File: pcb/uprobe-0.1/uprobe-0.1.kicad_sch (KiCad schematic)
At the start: 99 parts, among them J1 uConsoleEXT, J2 Conn_02x05_Odd_Even, J3 Conn_02x05_Odd_Even, J4 JST_SH_BM03B-SRSS, J5 Conn_01x02, J7 Conn_01x04, Q1 BSS138, Q7 DMG1024UV, Q8 DMG1023UV, SW1 XUNPU TS-1088-AR02016, SW2 XUNPU TS-1088-AR02016, U1 ATmega8A-M, U10 74LVC2T45DC, U11 74LVC2T45DC, U12 74LVC2T45DC, U2 AMS1117-3.3, U3 AP22653, U4 AP22653, U5 STM32F103CBUx, U6 74LVC2T45DC, U7 74LVC2T45DC, U8 74LVC2T45DC, U9 74LVC2T45DC, Y1 ABM8-12.000MHZ-B2-T, Y2 ABM8-8.000MHZ-B2-T

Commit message: layout update
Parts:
- added JP2: SolderJumper_3_Bridged12, Jumper:SolderJumper-3_P2.0mm_Open_TrianglePad1.0x1.5mm, symbol Jumper:SolderJumper_3_Bridged12
- added JP3: SolderJumper_2_Open, Jumper:SolderJumper-2_P1.3mm_Open_TrianglePad1.0x1.5mm, symbol Jumper:SolderJumper_2_Open
- added LD3, LD4: XL-3210SURUGC, uprobe:XL-3210SURUGC, symbol Device:LED_Dual_AKAK
- added R43, R44, R45, R46: 270, Resistor_SMD:R_0603_1608Metric, symbol Device:R
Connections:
- net BM_LED0: now also R43.2
- net BM_LED1: now also R45.2, R46.2
- net BM_LED2: now also R44.2
- net GND: now also JP2.1 (A), LD3.2 (K1), LD3.4 (K2), LD4.2 (K1), LD4.4 (K2); no longer J3.9 (Pin_9)
- net RST: now also RN2.3 (R3.1); no longer RN2.5 (R4.2)
- net RXD: now also RN2.2 (R2.1), JP2.3 (B); no longer RN2.7 (R2.2)
- net TCK: now also RN1.3 (R3.1); no longer RN1.6 (R3.2)
- net TDI: now also RN1.1 (R1.1); no longer RN1.8 (R1.2)
- net TDO: now also RN1.2 (R2.1); no longer RN1.7 (R2.2)
- net TMS: now also RN1.4 (R4.1); no longer RN1.5 (R4.2)
- net TPWR: now also RN2.4 (R4.1); no longer RN2.6 (R3.2)
- net TXD: now also RN2.1 (R1.1), JP3.2 (B); no longer RN2.8 (R1.2)
- net xRST: now also RN2.6 (R3.2); no longer RN2.4 (R4.1)
- net xRXD: now also RN2.7 (R2.2); no longer RN2.2 (R2.1)
- net xTCK: now also RN1.6 (R3.2); no longer RN1.3 (R3.1)
- net xTDI: now also RN1.8 (R1.2); no longer RN1.1 (R1.1)
- net xTDO: now also RN1.7 (R2.2); no longer RN1.2 (R2.1)
- net xTMS: now also RN1.5 (R4.2); no longer RN1.4 (R4.1)
- net xTPWR: now also RN2.5 (R4.2); no longer RN2.3 (R3.1)
- net xTXD: now also RN2.8 (R1.2); no longer RN2.1 (R1.1)
- net at J3.7 (Pin_7): now also JP3.1 (A)
- net TPWR_DTCT: now reaches C18.1, R33.1, R34.2, U5.18 (PB0)
- net UASP_MISO renamed xUASP_MISO
- net UASP_MISO* renamed iUASP_MISO
- net UASP_MOSI renamed xUASP_MOSI
- net UASP_MOSI* renamed iUASP_MOSI
- net UASP_RST renamed xUASP_RST
- net UASP_RST* renamed iUASP_RST
- net UASP_RX renamed xUASP_RX
- net UASP_RX* renamed iUASP_RX
- net UASP_SCK renamed xUASP_SCK
- net UASP_SCK* renamed iUASP_SCK
- net UASP_TX renamed xUASP_TX
- net UASP_TX* renamed iUASP_TX
- new net: LD3.1 (A1), R43.1
- new net: LD3.3 (A2), R44.1
- new net: J3.9 (Pin_9), JP2.2 (C)
- new net: LD4.3 (A2), R46.1
- new net: LD4.1 (A1), R45.1
- no-connect marks 31 -> 30
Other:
- note removed: "TODO: LEDS!!!"
- moved on the sheet: J7, LD1, R30, R31, R5, R6, RN1, RN2

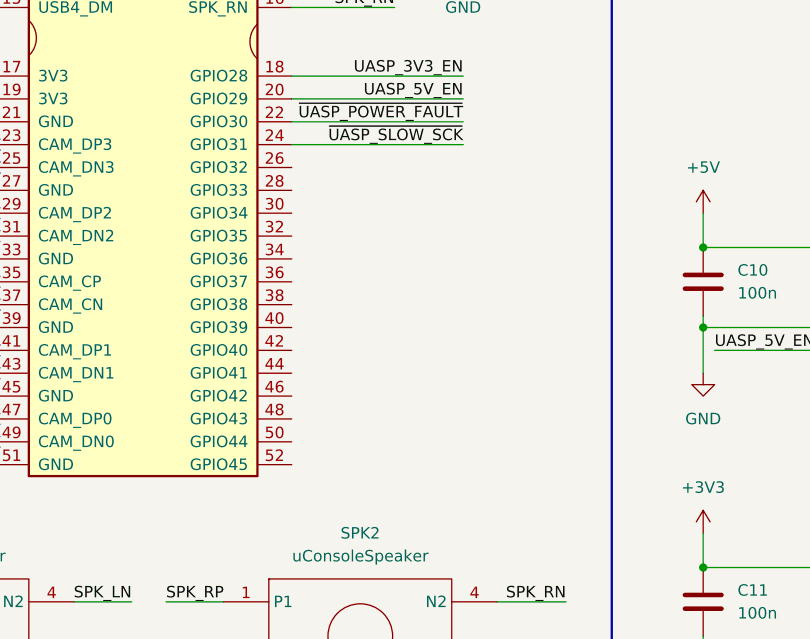
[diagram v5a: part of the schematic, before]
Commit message: additional gpio
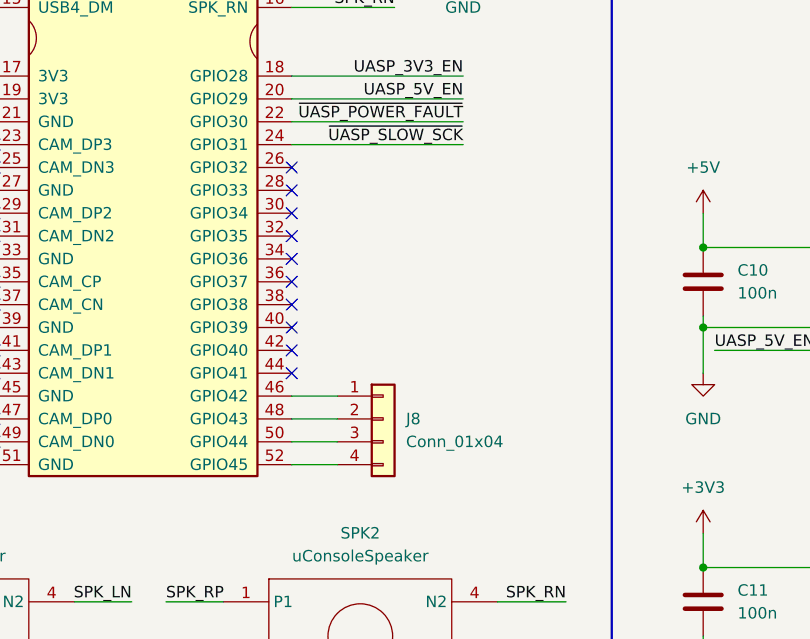
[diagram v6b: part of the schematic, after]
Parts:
- added J8: Conn_01x04, Connector_PinHeader_2.54mm:PinHeader_1x04_P2.54mm_Vertical, symbol Connector_Generic:Conn_01x04
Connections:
- net at J1.46 (GPIO42): now also J8.1 (Pin_1)
- net at J1.48 (GPIO43): now also J8.2 (Pin_2)
- net at J1.50 (GPIO44): now also J8.3 (Pin_3)
- net at J1.52 (GPIO45): now also J8.4 (Pin_4)
- no-connect marks 30 -> 40
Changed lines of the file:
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@@
 	)
 	(no_connect
+		(at 77.47 85.09)
+	)
+	(no_connect
 		(at 217.17 68.58)
 	)
@@
 	)
 	(no_connect
+		(at 77.47 74.93)
+	)
+	(no_connect
 		(at 44.45 64.77)
 	)
 	(no_connect
+		(at 77.47 69.85)
+	)
+	(no_connect
+		(at 77.47 87.63)
+	)
+	(no_connect
 		(at 247.65 78.74)
 	)
@@
 	)
 	(no_connect
+		(at 77.47 82.55)
+	)
+	(no_connect
 		(at 247.65 101.6)
 	)
@@
 	)
 	(no_connect
+		(at 77.47 90.17)
+	)
+	(no_connect
 		(at 247.65 81.28)
 	)
 	(no_connect
+		(at 77.47 67.31)
+	)
+	(no_connect
 		(at 151.13 229.87)
 	)
 	(no_connect
+		(at 77.47 80.01)
+	)
+	(no_connect
 		(at 151.13 196.85)
 	)
@@
 	)
 	(no_connect
+		(at 77.47 72.39)
+	)
+	(no_connect
 		(at 247.65 96.52)
 	)
@@
 	)
 	(no_connect
+		(at 77.47 77.47)
+	)
+	(no_connect
 		(at 186.69 217.17)
 	)
@@
 	(wire
 		(pts
+			(xy 77.47 95.25) (xy 82.55 95.25)
+		)
+		(stroke
+			(width 0)
+			(type default)
+		)
+	)
+	(wire
+		(pts
 			(xy 361.95 203.2) (xy 361.95 207.01)
 		)
@@
 	(wire
 		(pts
+			(xy 77.47 97.79) (xy 82.55 97.79)
+		)
+		(stroke
+			(width 0)
+			(type default)
+		)
+	)
+	(wire
+		(pts
 			(xy 30.48 85.09) (xy 30.48 92.71)
 		)
@@
 	(wire
 		(pts
+			(xy 77.47 92.71) (xy 82.55 92.71)
+		)
+		(stroke
+			(width 0)
+			(type default)
+		)
+	)
+	(wire
+		(pts
 			(xy 336.55 36.83) (xy 336.55 57.15)
 		)
@@
 	(wire
 		(pts
+			(xy 77.47 100.33) (xy 82.55 100.33)
+		)
+		(stroke
+			(width 0)
+			(type default)
+		)
+	)
+	(wire
+		(pts
 			(xy 321.31 31.75) (xy 321.31 29.21)
 		)
@@
 					(unit 1)
 				)
+			)
+		)
+	)
+	(symbol
+		(lib_id "Connector_Generic:Conn_01x04")
+		(at 87.63 95.25 0)
+		(unit 1)
+		(exclude_from_sim no)
+		(in_bom yes)
+		(on_board yes)
+		(dnp no)
+		(fields_autoplaced yes)
+		(property "Reference" "J8"
+			(at 90.17 95.2499 0)
+			(effects
+				(font
+					(size 1.27 1.27)
+				)
+				(justify left)
+			)
+		)
+		(property "Value" "Conn_01x04"
+			(at 90.17 97.7899 0)
+			(effects
+				(font
+					(size 1.27 1.27)
+				)
+				(justify left)
+			)
+		)
+		(property "Footprint" "Connector_PinHeader_2.54mm:PinHeader_1x04_P2.54mm_Vertical"
+			(at 87.63 95.25 0)
+			(effects
+				(font
+					(size 1.27 1.27)
+				)
+				(hide yes)
+			)
+		)
+		(property "Datasheet" "~"
+			(at 87.63 95.25 0)
+			(effects
+				(font
+					(size 1.27 1.27)
+				)
+				(hide yes)
+			)
+		)
+		(property "Description" "Generic connector, single row, 01x04, script generated (kicad-library-utils/schlib/autogen/connector/)"
+			(at 87.63 95.25 0)
+			(effects
+				(font
+					(size 1.27 1.27)
+				)
+				(hide yes)
+			)
+		)
+		(pin "1"
+		)
+		(pin "2"
+		)
+		(pin "3"
+		)
+		(pin "4"
+		)
+		(instances
+			(project ""
+				(path "/663115e4-0f28-4879-a79a-00db74a12eda"
+					(reference "J8")
+					(unit 1)
+				)

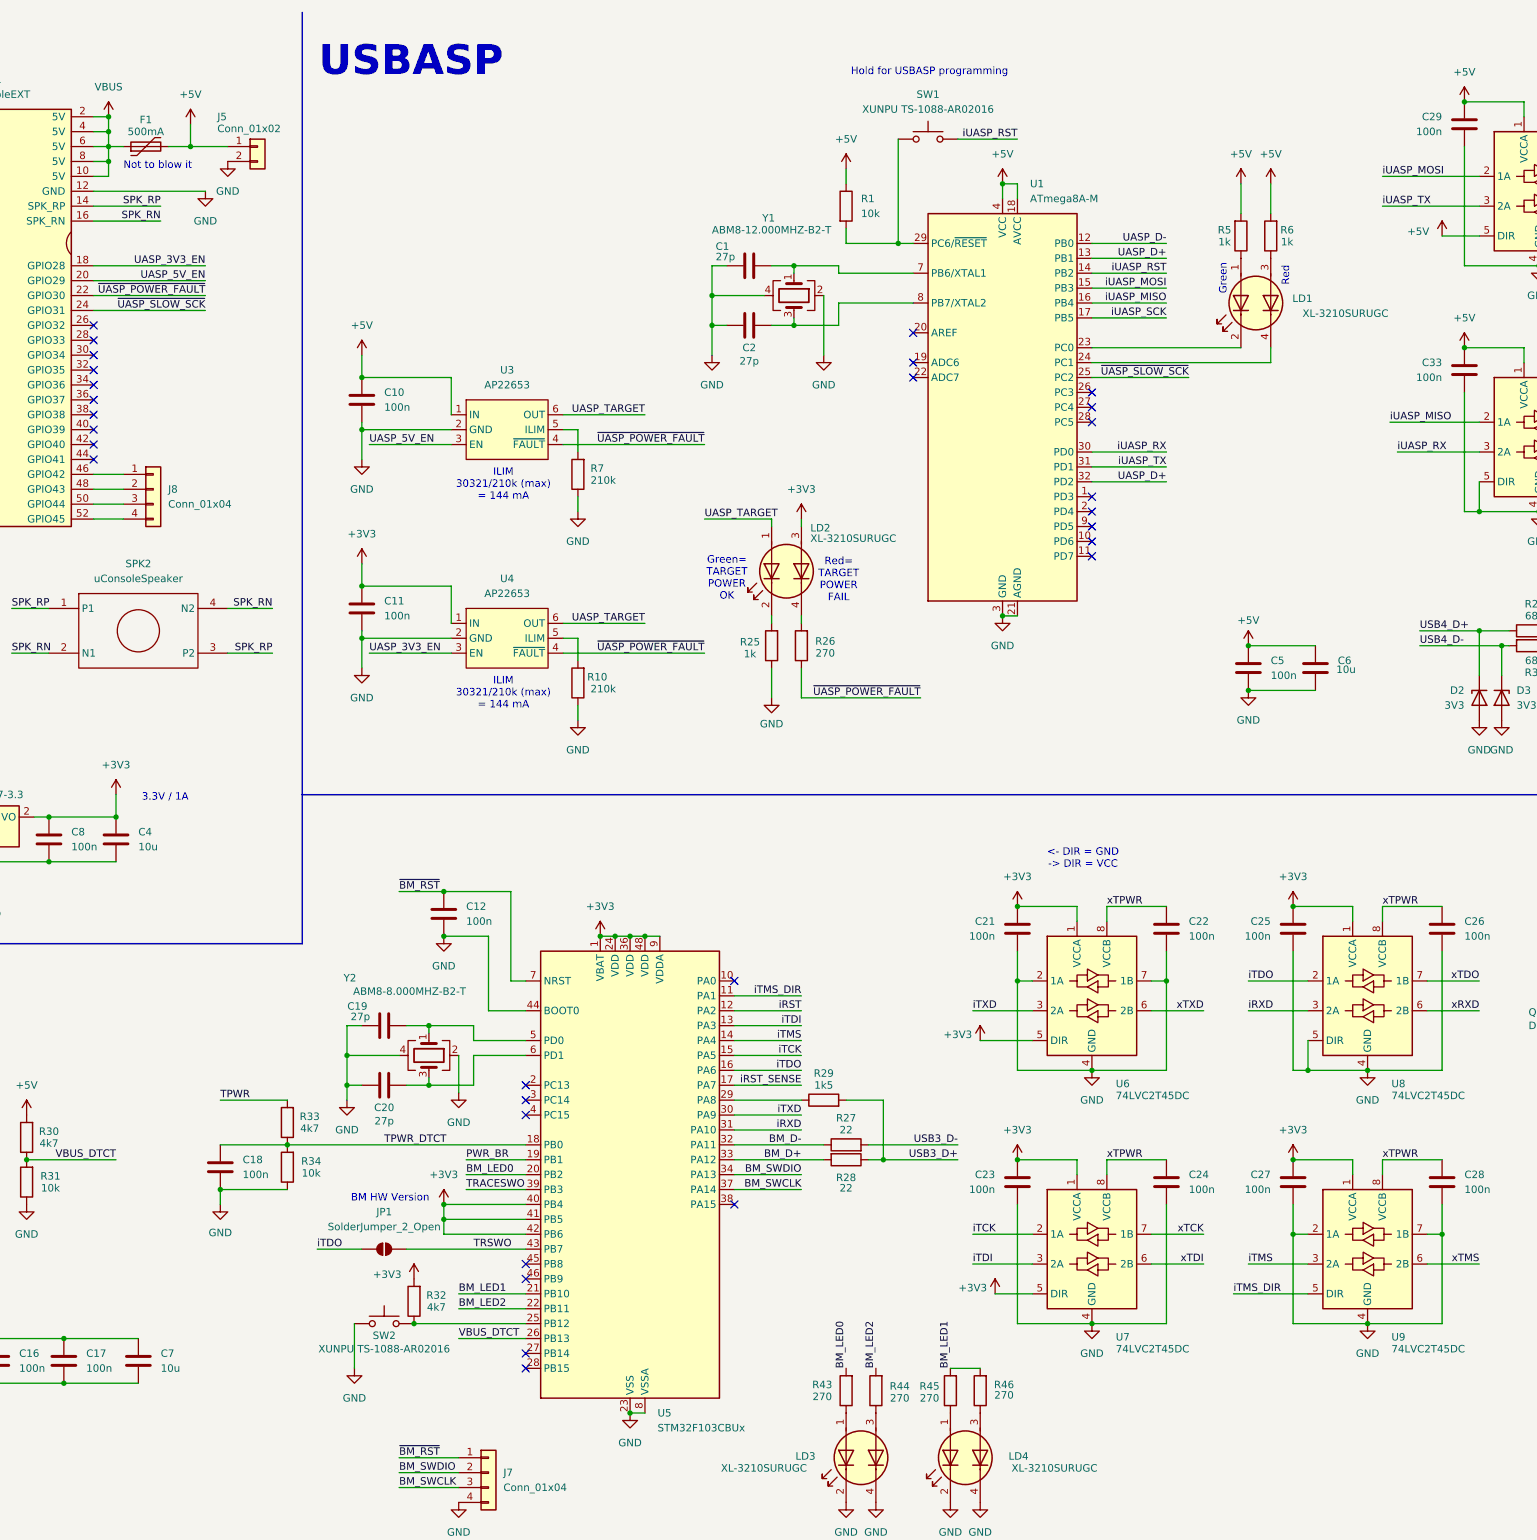
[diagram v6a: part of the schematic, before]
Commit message: schematic notes and power script for usbasp
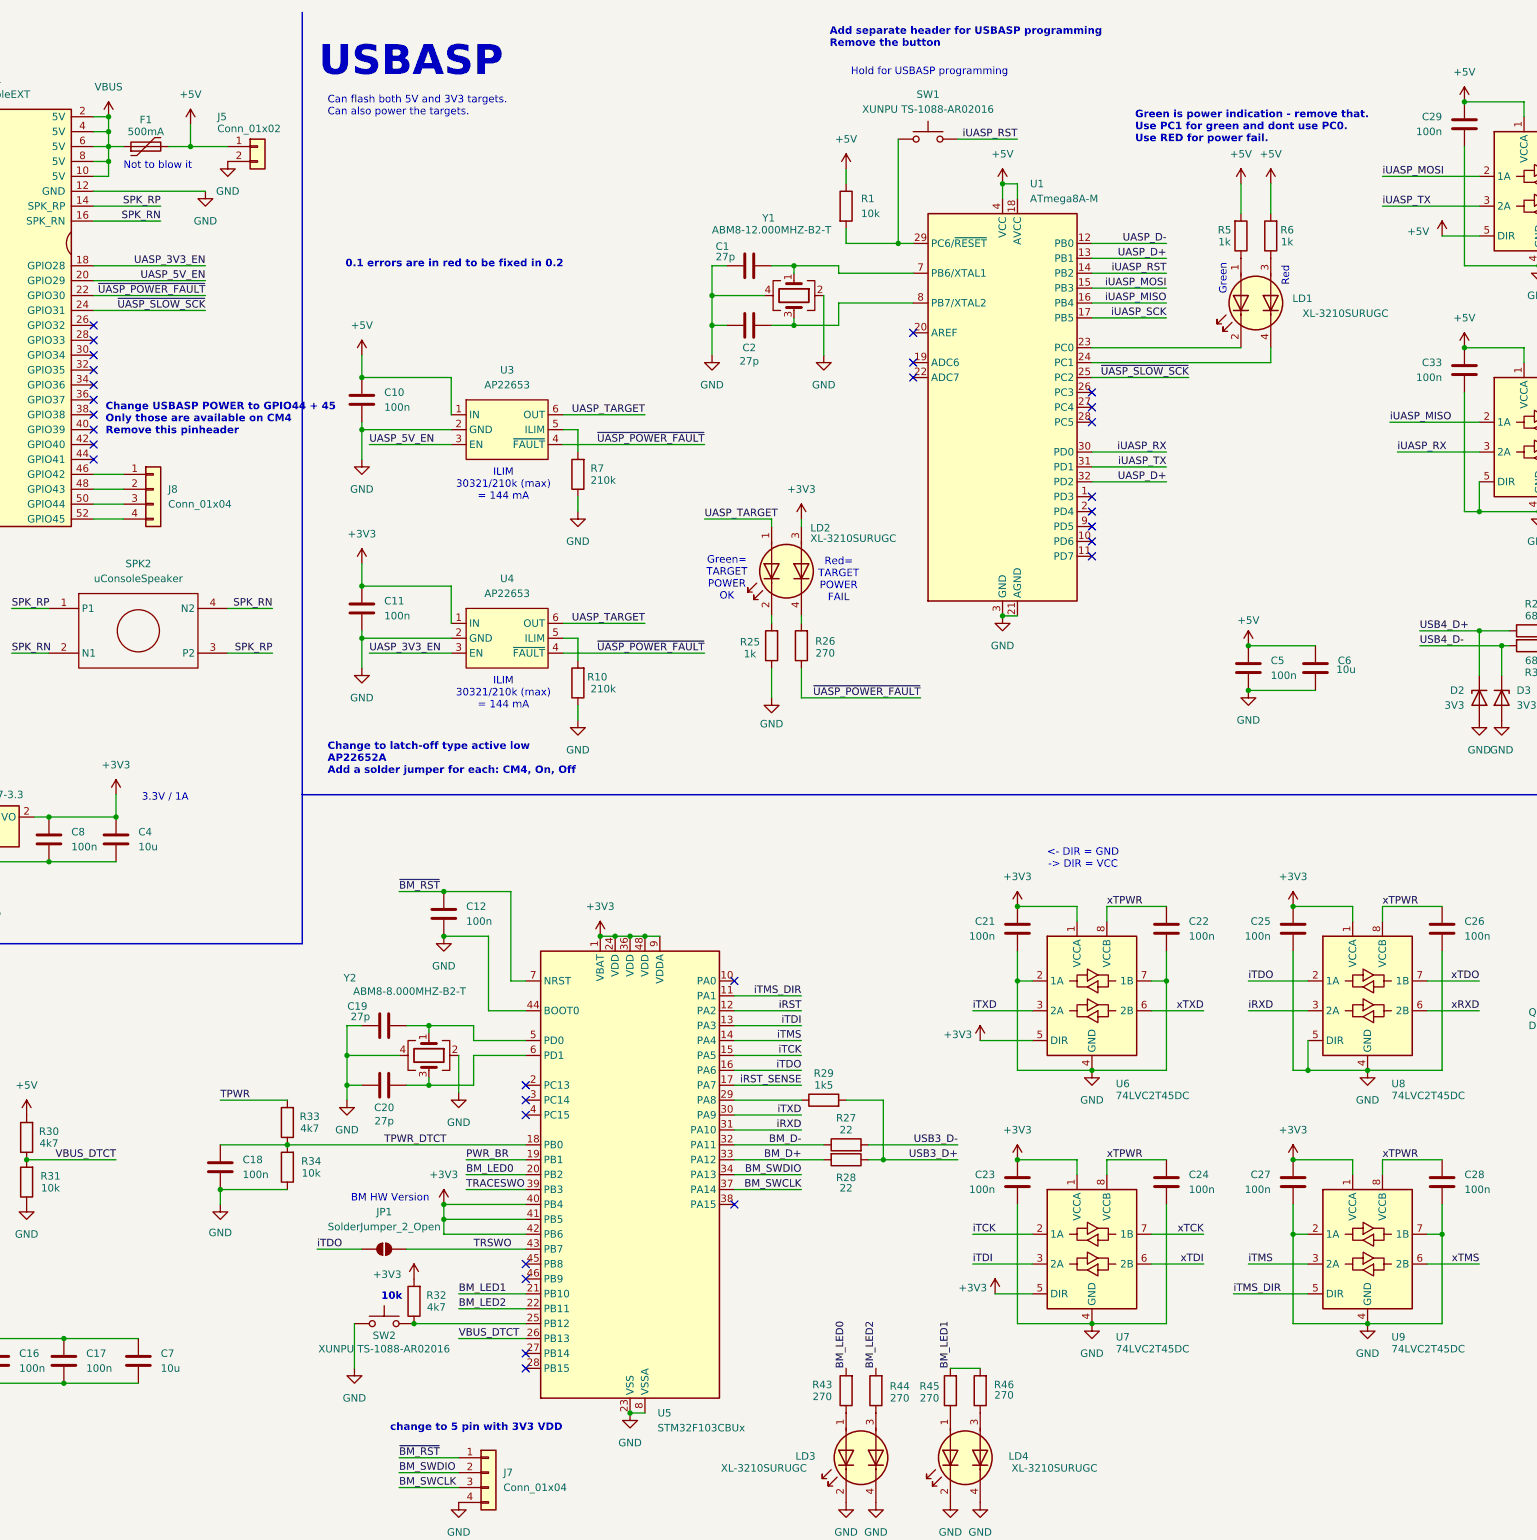
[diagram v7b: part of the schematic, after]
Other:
- note added: "0.1 errors are in red to be fixed in 0.2"
- note added: "10k"
- note added: "Add separate header for USBASP programming Remove the button"
- note added: "Can flash both 5V and 3V3 targets. Can also power the targets."
- note added: "Change USBASP POWER to GPIO44 + 45 Only those are available on CM4 Remove this pinheader"
- note added: "Change to latch-off type active low AP22652A Add a solder jumper for each: CM4, On, Off"
- note added: "Green is power indication - remove that. Use PC1 for green and dont use PC0. Use RED for power fail."
- note added: "change to 5 pin with 3V3 VDD"
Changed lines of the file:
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@@
+		)
+	)
+	(text "10k"
+		(exclude_from_sim no)
+		(at 126.492 232.918 0)
+		(effects
+			(font
+				(size 1.27 1.27)
+				(thickness 0.254)
+				(bold yes)
+				(color 255 0 0 1)
+			)
+			(justify left)
 		)
 	)
@@
 		)
 	)
+	(text "Can flash both 5V and 3V3 targets.\nCan also power the targets."
+		(exclude_from_sim no)
+		(at 117.348 29.972 0)
+		(effects
+			(font
+				(size 1.27 1.27)
+			)
+			(justify left)
+		)
+	)
+	(text "change to 5 pin with 3V3 VDD"
+		(exclude_from_sim no)
+		(at 128.016 255.27 0)
+		(effects
+			(font
+				(size 1.27 1.27)
+				(thickness 0.254)
+				(bold yes)
+				(color 255 0 0 1)
+			)
+			(justify left)
+		)
+	)
 	(text "COMMON"
 		(exclude_from_sim no)
@@
 		)
 	)
+	(text "Change to latch-off type active low\nAP22652A\nAdd a solder jumper for each: CM4, On, Off"
+		(exclude_from_sim no)
+		(at 117.348 141.224 0)
+		(effects
+			(font
+				(size 1.27 1.27)
+				(thickness 0.254)
+				(bold yes)
+				(color 255 0 0 1)
+			)
+			(justify left)
+		)
+	)
 	(text "BM HW Version"
 		(exclude_from_sim no)
@@
 		)
 	)
+	(text "Green is power indication - remove that.\nUse PC1 for green and dont use PC0.\nUse RED for power fail."
+		(exclude_from_sim no)
+		(at 255.016 33.528 0)
+		(effects
+			(font
+				(size 1.27 1.27)
+				(thickness 0.254)
+				(bold yes)
+				(color 255 0 0 1)
+			)
+			(justify left)
+		)
+	)
 	(text "Green"
 		(exclude_from_sim no)
@@
 		)
 	)
+	(text "0.1 errors are in red to be fixed in 0.2"
+		(exclude_from_sim no)
+		(at 120.396 56.896 0)
+		(effects
+			(font
+				(size 1.27 1.27)
+				(thickness 0.254)
+				(bold yes)
+				(color 255 0 0 1)
+			)
+			(justify left)
+		)
+	)
+	(text "Change USBASP POWER to GPIO44 + 45\nOnly those are available on CM4\nRemove this pinheader"
+		(exclude_from_sim no)
+		(at 79.502 83.312 0)
+		(effects
+			(font
+				(size 1.27 1.27)
+				(thickness 0.254)
+				(bold yes)
+				(color 255 0 0 1)
+			)
+			(justify left)
+		)
+	)
 	(text "Level conversion:\n5V (USBASP) <=> 3V3 (Target)"
 		(exclude_from_sim no)
@@
 		)
 	)
+	(text "Add separate header for USBASP programming\nRemove the button"
+		(exclude_from_sim no)
+		(at 202.946 18.288 0)
+		(effects
+			(font
+				(size 1.27 1.27)
+				(thickness 0.254)
+				(bold yes)
+				(color 255 0 0 1)
+			)
+			(justify left)
+		)
+	)
